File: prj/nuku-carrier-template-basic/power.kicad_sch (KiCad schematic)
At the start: 11 parts, among them U1 AP61302

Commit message: Route template.basic
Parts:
- R23: value 330 -> 1k; LCSC C25104 -> C11702
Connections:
- no-connect marks 1 -> 0
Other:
- note added: "All FPGA banks @ 3V3"

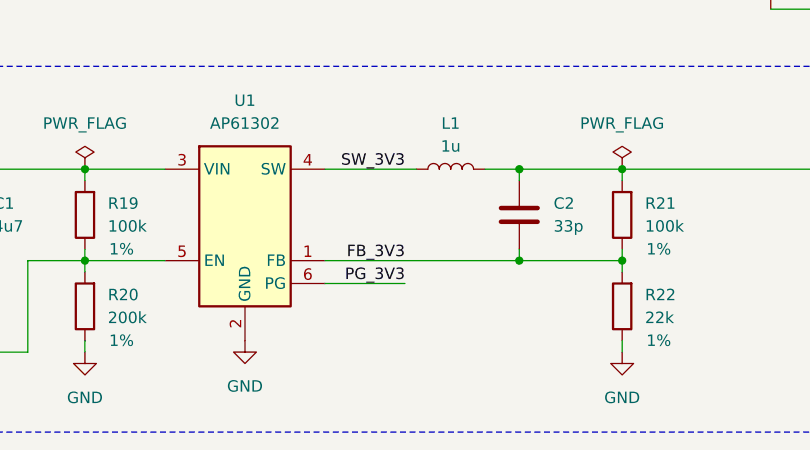
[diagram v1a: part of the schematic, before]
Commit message: Finish template.basic + Production outputs
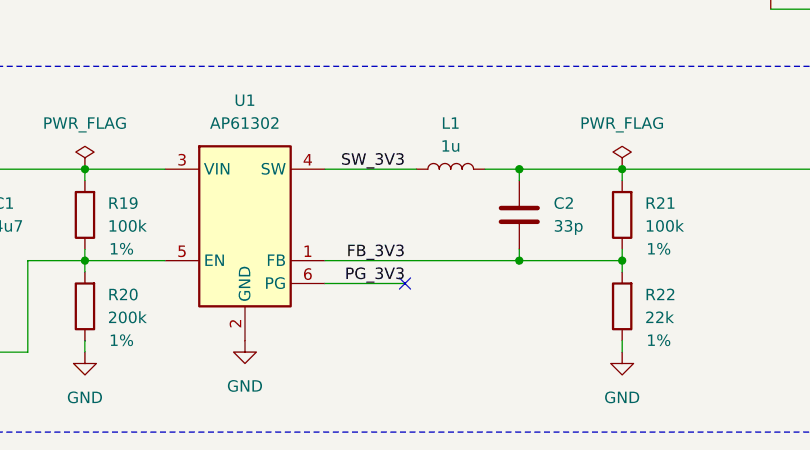
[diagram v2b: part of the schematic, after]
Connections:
- no-connect marks 0 -> 1
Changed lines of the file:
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@@
 		(color 0 0 0 0)
+	)
+	(no_connect
+		(at 135.89 107.95)
 	)
 	(wire

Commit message: Finish boards - prod ready
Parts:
- R20: now not fitted; now left out of the parts list
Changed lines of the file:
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@@
 		(unit 1)
 		(exclude_from_sim no)
-		(in_bom yes)
+		(in_bom no)
 		(on_board yes)
-		(dnp no)
+		(dnp yes)
 		(property "Reference" "R20"
 			(at 102.87 109.2199 0)
